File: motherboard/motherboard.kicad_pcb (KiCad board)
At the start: 4 copper layers, 142.2 x 209.6 mm, 507 parts, among them J1 Power In (Male-top), J10 Headset 1, J11 Device 1, J12 Headset 2, J13 Headset 3, J14 Headset 4, J15 Device 2, J16 Headset 5, J17 Headset 6, J18 Device 3, J19 Headset 7, J2 Power Out (Male-top), J20 I2C and RESET (Male-top), J21 Device 4, J22 Device 5, J23 Device 6, J24 5V-I2C-2, J25 5V-I2C-3, J26 5V-I2C-4, J27 5V-I2C-5, J28 5V-I2C-6, J29 Device 7, J3 GND (Male-top), J30 Output to Mixer, J4 MIC-IN (Male-top), J5 Headphone Audio Out (Male-top), J6 Headphone Audio In (Male-top), J7 MIC-OUT (Male-top), J8 Device 0, J9 Headset 0, U1 LM27762, U10 ADG708, U11 ADG708, U12 ADG708, U13 ADG708, U14 TCA9555, U15 ADG708, U16 ADG708, U17 TCA9548A, U18 ADG708, U19 TCA9555, U2 74ACT32, U20 ADG708, U21 TCA9555, U22 OPA1604, U23 DS1882, U24 OPA1604, U25 DS1882, U26 OPA1604, U27 DS1882, U28 OPA1604, U29 DS1882, U3 TS12A44514, U30 OPA1604, U31 DS1882, U32 OPA1604, U33 DS1882, U34 OPA1604, U35 DS1882, U36 OPA1604, U37 DS1882, U38 OPA1602, U39 OPA1604, U4 LMZ34002, U40 OPA1602, U41 OPA1604, U42 OPA1602, U43 OPA1604, U44 OPA1602, U45 OPA1604, U46 OPA1602, U47 OPA1604, U48 OPA1602, U49 OPA1604, U5 LM1085-12V, U50 OPA1602, U51 OPA1604, U52 OPA1602, U53 OPA1604, U6 TS12A44514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

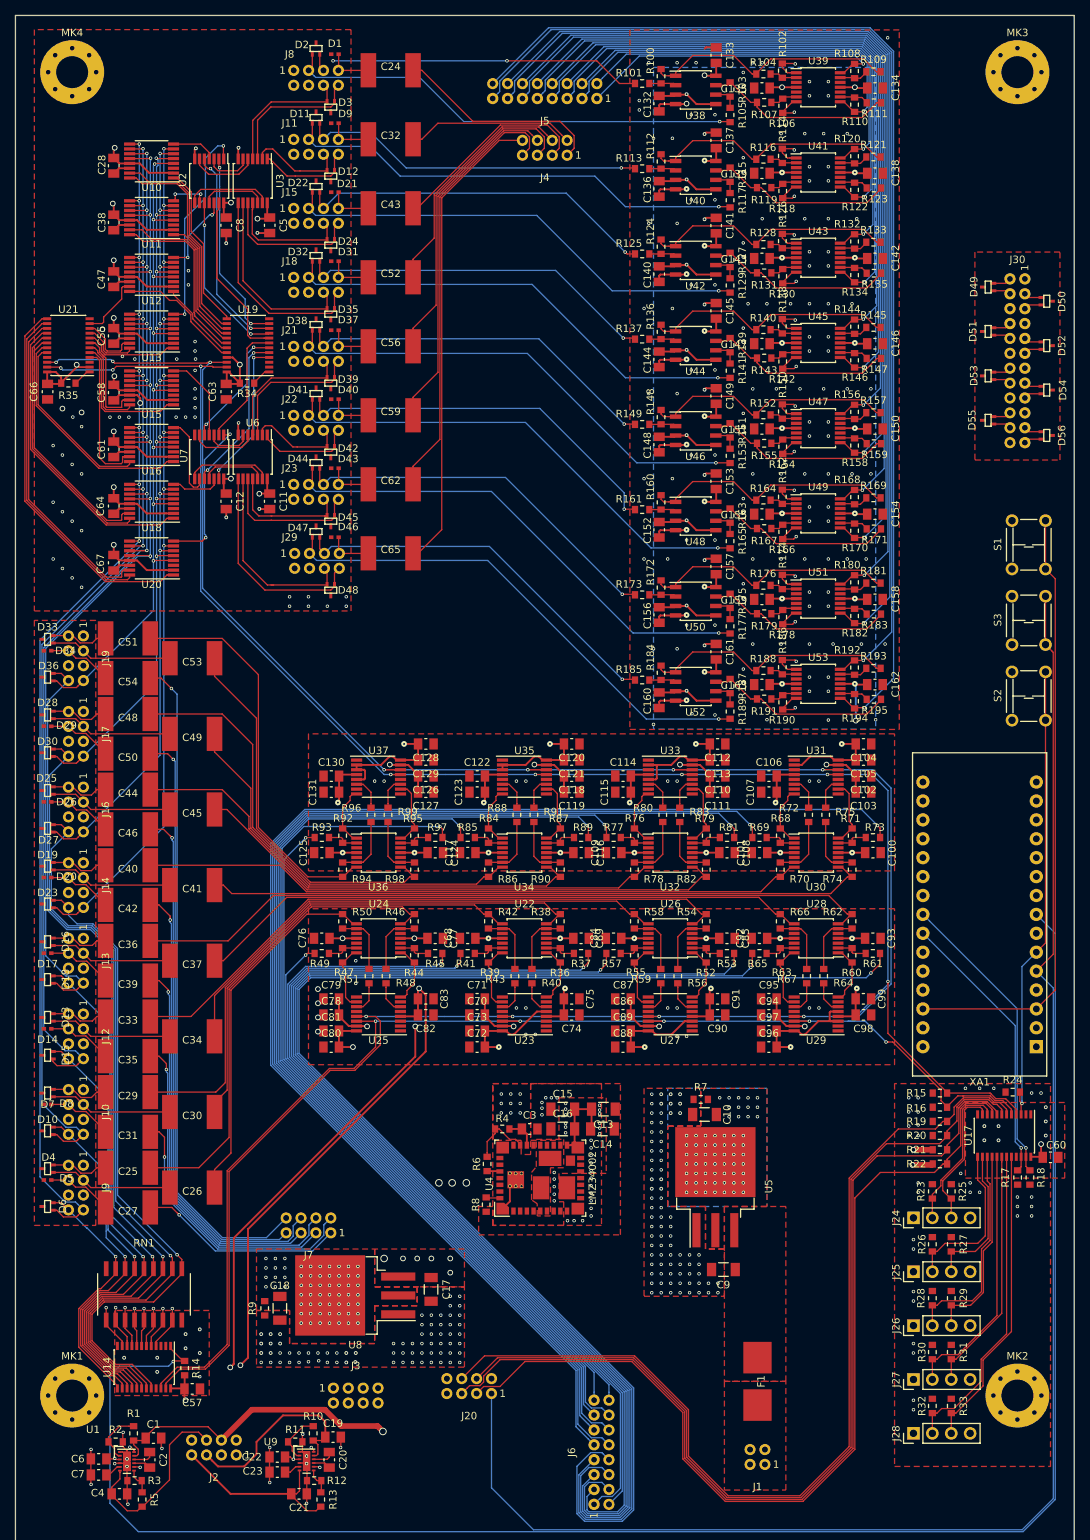
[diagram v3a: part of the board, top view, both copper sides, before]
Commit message: Rotating device connectors
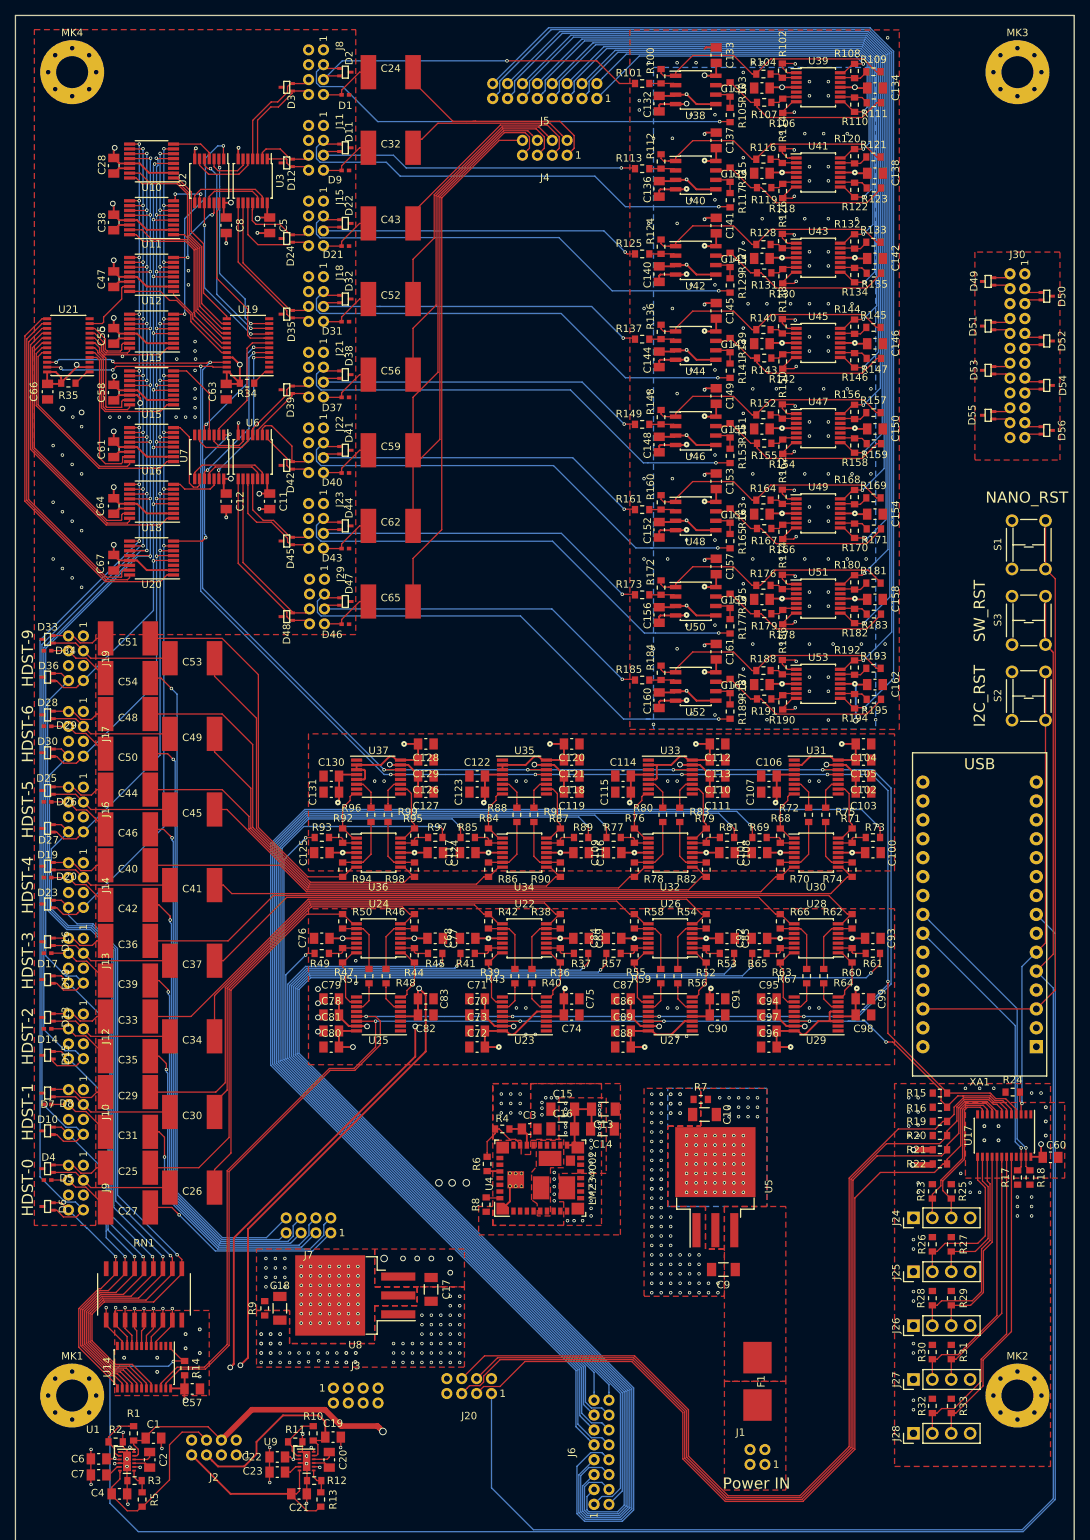
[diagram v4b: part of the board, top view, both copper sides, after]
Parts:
- moved D46 11.8 mm to (100.2, 188.5), turned to 0 degrees
- moved D43 10.9 mm to (100.2, 178.3), turned to 0 degrees
- moved D47 10.2 mm to (100.2, 185.4), turned to 270 degrees
- moved D40 10.0 mm to (100.2, 168.1), turned to 0 degrees
- moved D44 9.38 mm to (100.2, 175.3), turned to 270 degrees
- moved D37 9.12 mm to (100.2, 158.0), turned to 0 degrees
- moved D41 8.58 mm to (100.2, 165.1), turned to 270 degrees
- moved D31 8.25 mm to (100.2, 147.8), turned to 0 degrees
- moved D38 7.80 mm to (100.2, 154.9), turned to 270 degrees
- moved D21 7.37 mm to (100.2, 137.7), turned to 0 degrees
- moved D32 7.04 mm to (100.2, 144.8), turned to 270 degrees
- moved D48 6.90 mm to (92.3, 187.5), turned to 90 degrees
- moved D9 6.50 mm to (100.2, 127.5), turned to 0 degrees
- moved D3 6.49 mm to (92.3, 116.3), turned to 90 degrees
- moved D45 6.49 mm to (92.3, 177.3), turned to 90 degrees
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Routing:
- net /Audio Mux and Control/MIXER-OUT-L-6: track 44.9 -> 55.0 mm
- net /Audio Mux and Control/MIXER-OUT-L-7: track 54.3 -> 64.0 mm
- net /Audio Mux and Control/MIXER-OUT-R-5: track 45.4 -> 54.9 mm
- net /Audio Mux and Control/PTT-DEV4: track 19.2 -> 9.91 mm
- net /Audio Mux and Control/MIXER-OUT-R-6: track 50.0 -> 57.9 mm
- net /Audio Mux and Control/PTT+DEV4: track 18.6 -> 11.3 mm
- net /Audio Mux and Control/PTT-DEV3: track 28.2 -> 21.0 mm
- net /Audio Mux and Control/MIC-OUT7: track 63.8 -> 69.9 mm
- net /Audio Mux and Control/PTT+DEV2: track 17.0 -> 11.0 mm
- net /Audio Mux and Control/PTT-DEV1: track 12.8 -> 6.81 mm
- net /Audio Mux and Control/PTT+DEV3: track 25.8 -> 19.8 mm
- net /Audio Mux and Control/PTT-DEV2: track 19.3 -> 13.3 mm
- net /Audio Mux and Control/MIC-OUT6: track 58.8 -> 64.4 mm
- net /Audio Mux and Control/PTT+DEV1: track 13.4 -> 8.05 mm
- net /Audio Mux and Control/PTT-DEV0: track 19.1 -> 14.1 mm
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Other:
- board text added: "HDST-0"
- board text added: "HDST-1"
- board text added: "HDST-2"
- board text added: "HDST-3"
- board text added: "HDST-4"
- board text added: "HDST-5"
- board text added: "HDST-6"
- board text added: "HDST-9"
- board text added: "I2C_RST"
- board text added: "NANO_RST"
- board text added: "Power IN"
- board text added: "SW_RST"
- board text added: "USB"
